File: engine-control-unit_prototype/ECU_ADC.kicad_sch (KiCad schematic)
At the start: 30 parts, among them J4 VREF, J5 PT1, J6 PT1, J7 VREF, U1 INA826, U4 INA826

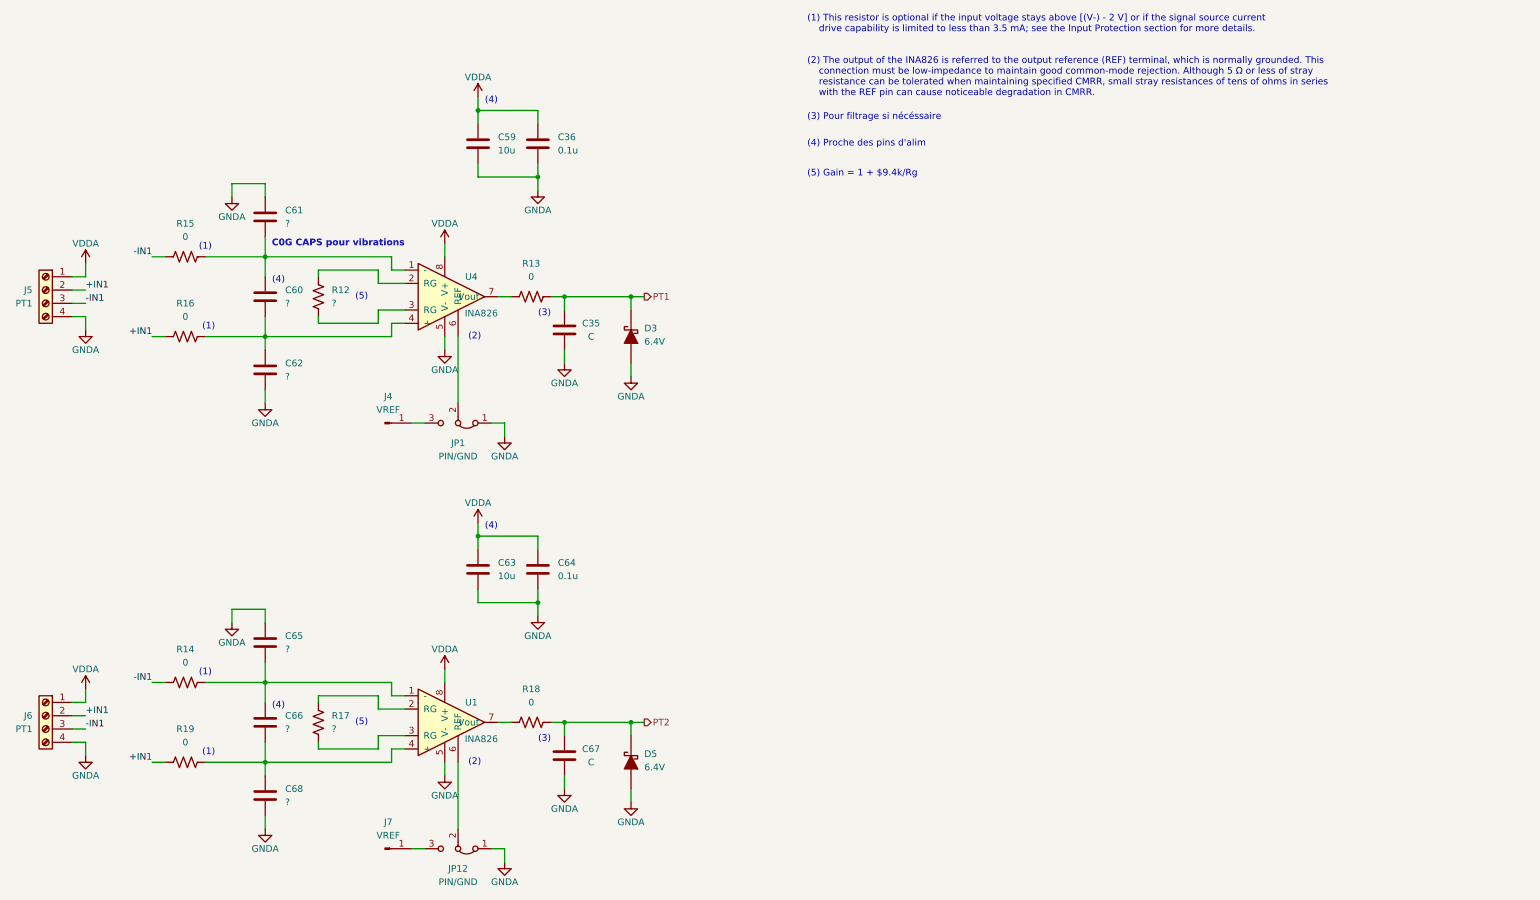
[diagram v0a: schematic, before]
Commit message: Added power circuitry without components values
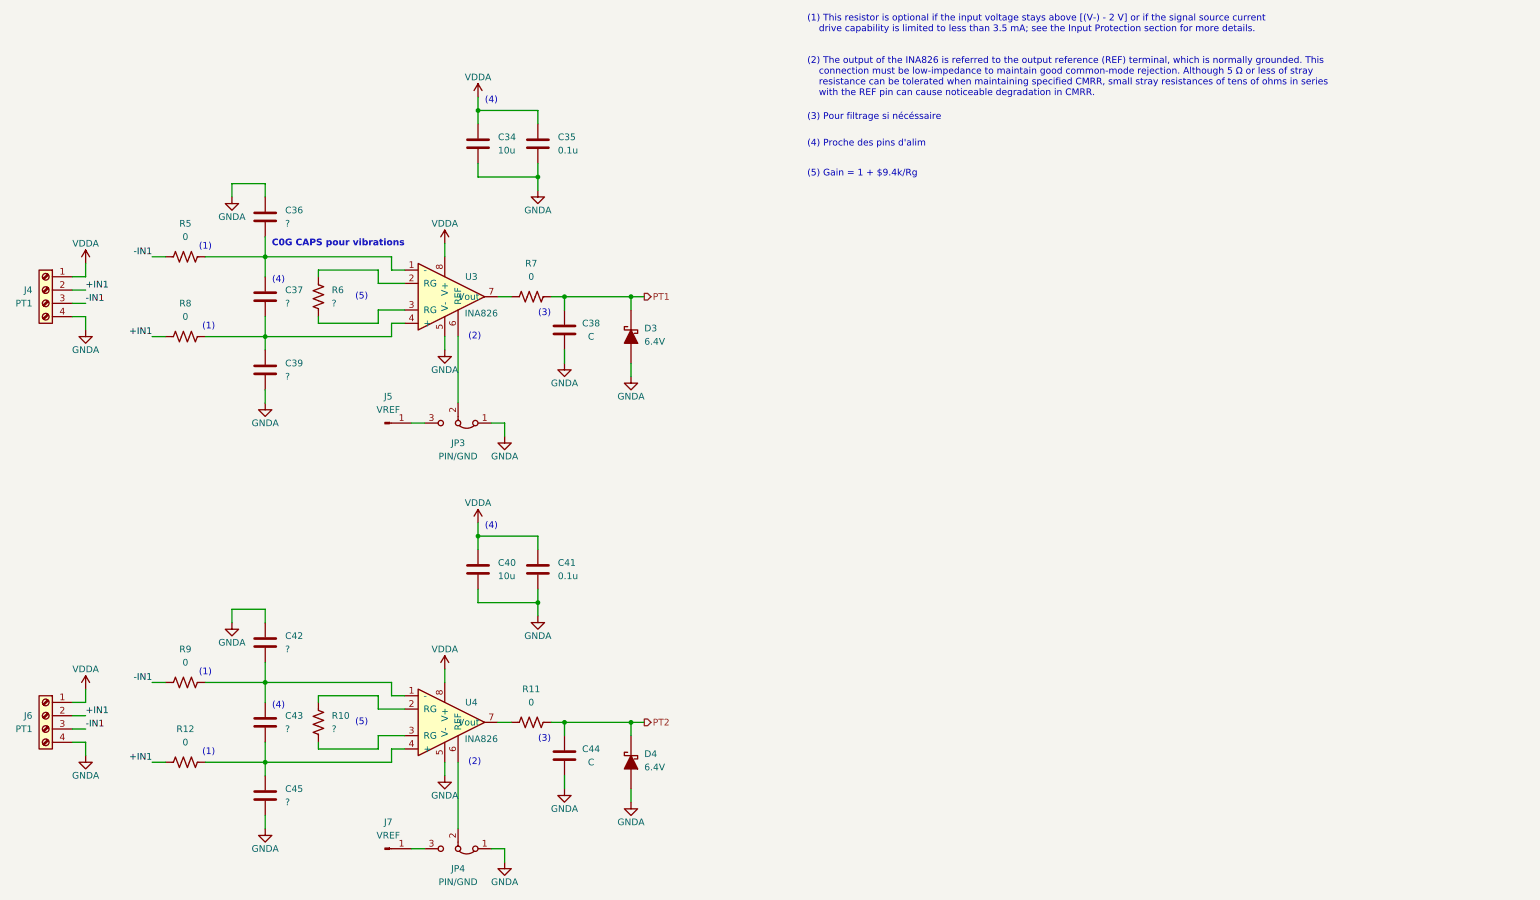
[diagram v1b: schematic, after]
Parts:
- renumbered C59 to C34, C36 to C35, C61 to C36, C60 to C37, C35 to C38, C62 to C39, C63 to C40, C64 to C41, C65 to C42, C66 to C43, C67 to C44, C68 to C45, D5 to D4, J5 to J4, J4 to J5, JP1 to JP3, JP12 to JP4, R17 to R10, R18 to R11, R19 to R12, R15 to R5, R12 to R6, R13 to R7, R16 to R8, R14 to R9, U4 to U3, U1 to U4

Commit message: Modified SD card Fixed INA826 decoupling caps Removed reset button Added Ports connectors (headers for ease of access)
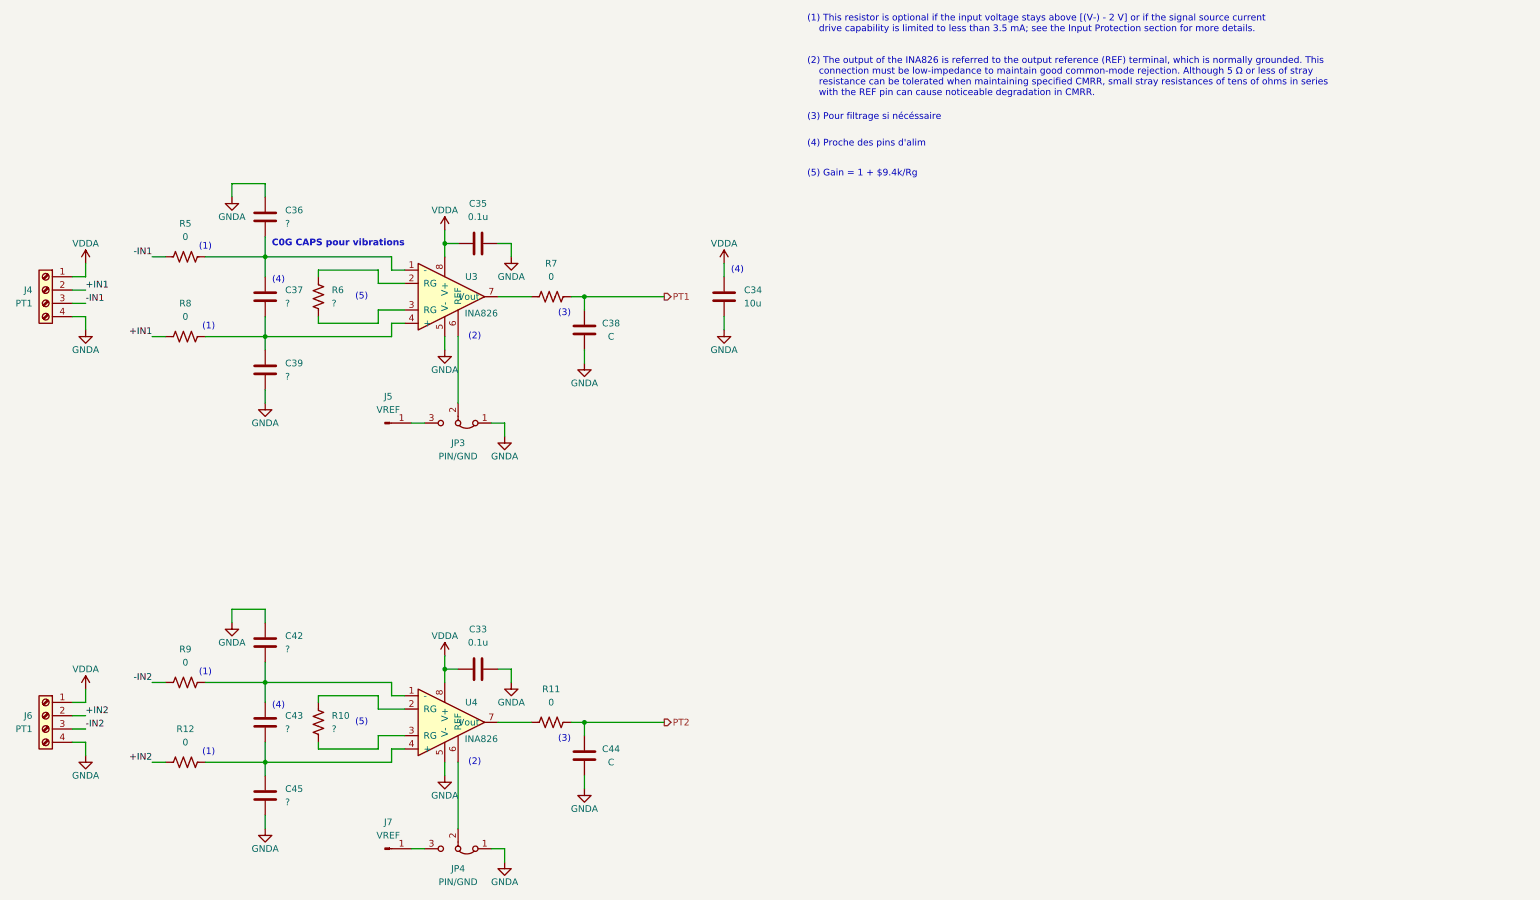
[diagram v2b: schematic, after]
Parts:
- removed C40: 10u, symbol Device:C
- removed C41: 0.1u, symbol Device:C
- removed D3, D4: 6.4V, Diode_SMD:D_0603_1608Metric_Pad1.05x0.95mm_HandSolder, symbol 0CSL_D1_V1:DIODE_SCHOTTKY_30V_200mA
- added C33: 0.1u, symbol Device:C
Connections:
- net +IN1: no longer J6.2 (Pin_2), R12.2
- net -IN1: no longer J6.3 (Pin_3), R9.2
- net GNDA: now also C33.1
- net VDDA: now also C33.2
- new net +IN2: J6.2 (Pin_2), R12.2
- new net -IN2: J6.3 (Pin_3), R9.2
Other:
- moved on the sheet: C34, C35, C38, C44, R11, R7

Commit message: Removed bloat libraries Changed symbols for Sirius custom library Changed layout for one page
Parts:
- removed C33, C35: 0.1u, symbol Device:C
- removed C34: 10u, symbol Device:C
- removed C36, C37, C39, C42, C43, C45: ?, symbol Device:C
- removed C38, C44: C, symbol Device:C
- removed J4, J6: PT1, symbol Connector:Screw_Terminal_01x04
- removed J5, J7: VREF, symbol Connector:Conn_01x01_Pin
- removed JP3, JP4: PIN/GND, symbol Jumper:Jumper_3_Bridged12
- removed R10, R6: ?, symbol Device:R_US
- removed R11, R12, R5, R7, R8, R9: 0, symbol Device:R_US
- removed U3, U4: INA826, UserFootprints:SOP65P490X110-8N, symbol INA826:INA826AIDGKR
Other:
- note removed: "(1)"
- note removed: "(1) This resistor is optional if the input voltage stays above [(V-) - 2 V] or if the signal source current drive capability is limited to less than 3.5 mA; see the Input Protection section for more details."
- note removed: "(2)"
- note removed: "(2) The output of the INA826 is referred to the output reference (REF) terminal, which is normally grounded. This connection must be low-impedance to maintain good common-mode rejection. Although 5 Ω or less of stray resistance can be tolerated when maintaining specified CMRR, small stray resistances of tens of ohms in series with the REF pin can cause noticeable degradation in CMRR."
- note removed: "(3)"
- note removed: "(3) Pour filtrage si nécéssaire"
- note removed: "(4)"
- note removed: "(4) Proche des pins d'alim"
- note removed: "(5)"
- note removed: "(5) Gain = 1 + $9.4k/Rg"
- note removed: "C0G CAPS pour vibrations"
